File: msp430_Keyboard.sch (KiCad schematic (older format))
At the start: 10 parts, among them SW14 L_Super, SW4 L_Ctrl, SW48 R_Ctrl, SW5 L_Shift, SW53 R_Shift, SW57 Alt_GR, SW60 R_Super, SW61 FUNC, SW9 L_Alt, U1 MSP430F5510IRGZ

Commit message: USB-Connector und Vogelfutter
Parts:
- added C? (x2): C_Small, symbol Device:C_Small
- added J?: Conn_01x04_Male, symbol Connector:Conn_01x04_Male
- added R?: R_Small, symbol Device:R_Small
- added Y? (x2): Crystal_Small, symbol Device:Crystal_Small
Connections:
- net GND: now also U1.10 (AVSS1), U1.12 (DVSS1), U1.27 (DVSS2), U1.37 (VSSU), U1.44 (AVSS2), C?.2, C?.2, J?.4 (Pin_4)
- net +3V3: now reaches U1.11 (DVCC1)
- net +3V3: now also U1.28 (DVCC2), U1.42 (VUSB), U1.7 (AVCC1), J?.1 (Pin_1)
- net USB/D+: now reaches U1.38 (PU.0/DP)
- net USB/D+: now also R?.2
- net at U1.39 (PUR): now also R?.1
- net USB/D-: now reaches U1.40 (PU.1/DM)
- net VBUS: now reaches U1.41 (VBUS)
- net at U1.45 (P5.2/XT2IN): now also C?.1, Y?.1
- net at U1.46 (P5.3/XT2OUT): now also C?.1, Y?.2
- net at U1.47 (SBWTCK/TEST): now also J?.2 (Pin_2)
- net at U1.48 (~RST~/NMI/SBWTDIO): now also J?.3 (Pin_3)
- net at U1.8 (P5.4/XIN): now also Y?.1
- net at U1.9 (P5.5/XOUT): now also Y?.2

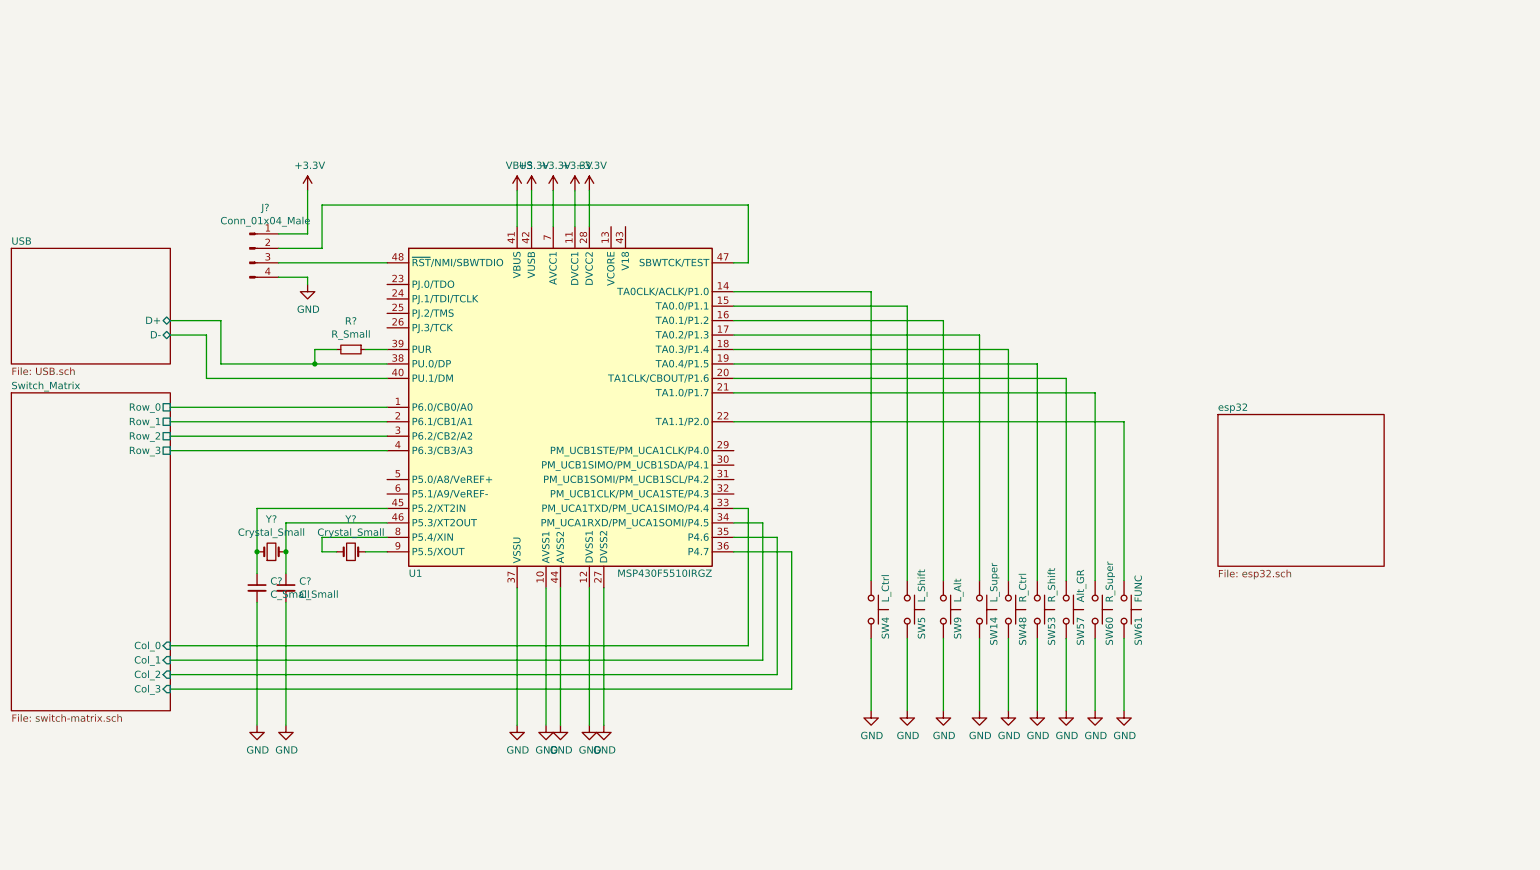
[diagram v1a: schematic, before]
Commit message: USB-Part und ESP32
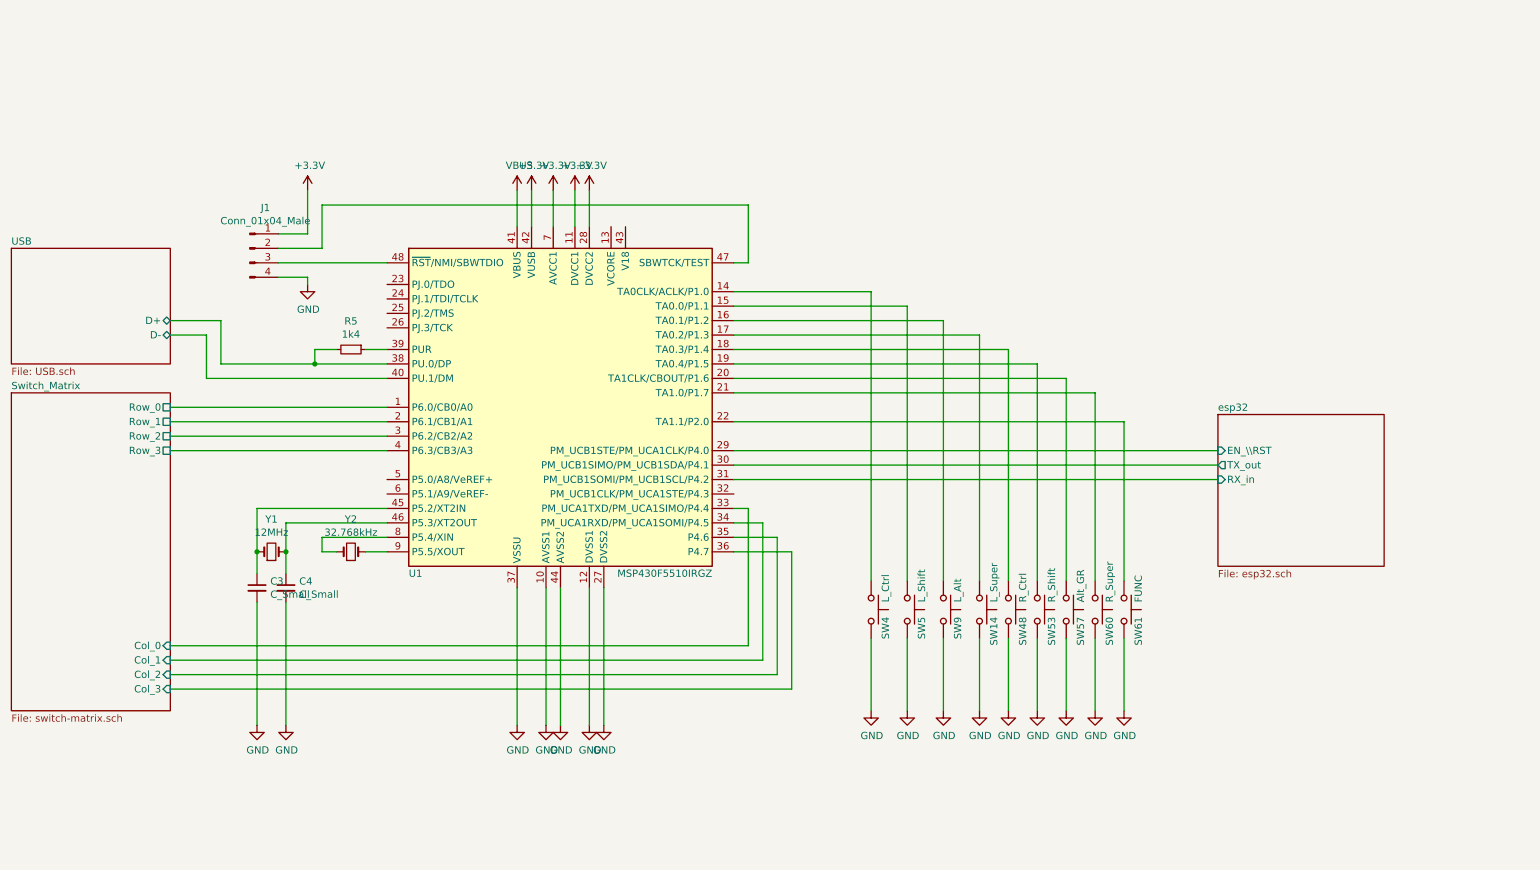
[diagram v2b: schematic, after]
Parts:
- C3, C4: renamed from C?; footprint (none) -> Capacitor_SMD:C_0603_1608Metric
- J1: renamed from J?; footprint (none) -> Connector_PinHeader_1.27mm:PinHeader_1x04_P1.27mm_Horizontal
- R5: renamed from R?; value R_Small -> 1k4; footprint (none) -> Resistor_SMD:R_0603_1608Metric
- Y1: renamed from Y?; value Crystal_Small -> 12MHz; footprint (none) -> Crystal:Crystal_SMD_EuroQuartz_MT-4Pin_3.2x2.5mm_HandSoldering
- Y2: renamed from Y?; value Crystal_Small -> 32.768kHz; footprint (none) -> Crystal:Crystal_SMD_MicroCrystal_MS3V-T1R
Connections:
- net esp32/EN_\\RST: now reaches U1.29 (PM_UCB1STE/PM_UCA1CLK/P4.0)
- net esp32/TX_out: now reaches U1.30 (PM_UCB1SIMO/PM_UCB1SDA/P4.1)
- net esp32/RX_in: now reaches U1.31 (PM_UCB1SOMI/PM_UCB1SCL/P4.2)
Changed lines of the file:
@@
 $Descr A4 11693 8268
 encoding utf-8
-Sheet 1 3
+Sheet 1 4
 Title ""
 Date ""
@@
 	2100 3450 2750 3450
 $Comp
-L power:GND #PWR?
+L power:GND #PWR0107
 U 1 1 60C6E7A3
 P 4150 5950
-F 0 "#PWR?" H 4150 5700 50  0001 C CNN
+F 0 "#PWR0107" H 4150 5700 50  0001 C CNN
 F 1 "GND" H 4155 5777 50  0000 C CNN
 F 2 "" H 4150 5950 50  0001 C CNN
@@
 $EndComp
 $Comp
-L power:GND #PWR?
+L power:GND #PWR0108
 U 1 1 60C6EAB5
 P 4350 5950
-F 0 "#PWR?" H 4350 5700 50  0001 C CNN
+F 0 "#PWR0108" H 4350 5700 50  0001 C CNN
 F 1 "GND" H 4355 5777 50  0000 C CNN
 F 2 "" H 4350 5950 50  0001 C CNN
@@
 $EndComp
 $Comp
-L power:GND #PWR?
+L power:GND #PWR0109
 U 1 1 60C6EDE3
 P 4450 5950
-F 0 "#PWR?" H 4450 5700 50  0001 C CNN
+F 0 "#PWR0109" H 4450 5700 50  0001 C CNN
 F 1 "GND" H 4455 5777 50  0000 C CNN
 F 2 "" H 4450 5950 50  0001 C CNN
@@
 $EndComp
 $Comp
-L power:GND #PWR?
+L power:GND #PWR0110
 U 1 1 60C6F39B
 P 4650 5950
-F 0 "#PWR?" H 4650 5700 50  0001 C CNN
+F 0 "#PWR0110" H 4650 5700 50  0001 C CNN
 F 1 "GND" H 4655 5777 50  0000 C CNN
 F 2 "" H 4650 5950 50  0001 C CNN
@@
 $EndComp
 $Comp
-L power:GND #PWR?
+L power:GND #PWR0111
 U 1 1 60C6F780
 P 4750 5950
-F 0 "#PWR?" H 4750 5700 50  0001 C CNN
+F 0 "#PWR0111" H 4750 5700 50  0001 C CNN
 F 1 "GND" H 4755 5777 50  0000 C CNN
 F 2 "" H 4750 5950 50  0001 C CNN
@@
 	4150 5950 4150 5000
 $Comp
-L Device:Crystal_Small Y?
+L Device:Crystal_Small Y2
 U 1 1 60C751AE
 P 3000 4750
-F 0 "Y?" H 3000 4975 50  0000 C CNN
-F 1 "Crystal_Small" H 3000 4884 50  0000 C CNN
-F 2 "" H 3000 4750 50  0001 C CNN
+F 0 "Y2" H 3000 4975 50  0000 C CNN
+F 1 "32.768kHz" H 3000 4884 50  0000 C CNN
+F 2 "Crystal:Crystal_SMD_MicroCrystal_MS3V-T1R" H 3000 4750 50  0001 C CNN
 F 3 "~" H 3000 4750 50  0001 C CNN
 	1    3000 4750
@@
 $EndComp
 $Comp
-L Device:Crystal_Small Y?
+L Device:Crystal_Small Y1
 U 1 1 60C76001
 P 2450 4750
-F 0 "Y?" H 2450 4975 50  0000 C CNN
-F 1 "Crystal_Small" H 2450 4884 50  0000 C CNN
-F 2 "" H 2450 4750 50  0001 C CNN
+F 0 "Y1" H 2450 4975 50  0000 C CNN
+F 1 "12MHz" H 2450 4884 50  0000 C CNN
+F 2 "Crystal:Crystal_SMD_EuroQuartz_MT-4Pin_3.2x2.5mm_HandSoldering" H 2450 4750 50  0001 C CNN
 F 3 "~" H 2450 4750 50  0001 C CNN
 	1    2450 4750
@@
 	2350 4450 2350 4750
 $Comp
-L Device:C_Small C?
+L Device:C_Small C3
 U 1 1 60C7B835
 P 2350 5000
-F 0 "C?" H 2442 5046 50  0000 L CNN
+F 0 "C3" H 2442 5046 50  0000 L CNN
 F 1 "C_Small" H 2442 4955 50  0000 L CNN
-F 2 "" H 2350 5000 50  0001 C CNN
+F 2 "Capacitor_SMD:C_0603_1608Metric" H 2350 5000 50  0001 C CNN
 F 3 "~" H 2350 5000 50  0001 C CNN
 	1    2350 5000
@@
 $EndComp
 $Comp
-L Device:C_Small C?
+L Device:C_Small C4
 U 1 1 60C7BD8A
 P 2550 5000
-F 0 "C?" H 2642 5046 50  0000 L CNN
+F 0 "C4" H 2642 5046 50  0000 L CNN
 F 1 "C_Small" H 2642 4955 50  0000 L CNN
-F 2 "" H 2550 5000 50  0001 C CNN
+F 2 "Capacitor_SMD:C_0603_1608Metric" H 2550 5000 50  0001 C CNN
 F 3 "~" H 2550 5000 50  0001 C CNN
 	1    2550 5000
@@
 Connection ~ 2550 4750
 $Comp
-L power:GND #PWR?
+L power:GND #PWR0112
 U 1 1 60C7EDC5
 P 2350 5950
-F 0 "#PWR?" H 2350 5700 50  0001 C CNN
+F 0 "#PWR0112" H 2350 5700 50  0001 C CNN
 F 1 "GND" H 2355 5777 50  0000 C CNN
 F 2 "" H 2350 5950 50  0001 C CNN
@@
 $EndComp
 $Comp
-L power:GND #PWR?
+L power:GND #PWR0113
 U 1 1 60C7F433
 P 2550 5950
-F 0 "#PWR?" H 2550 5700 50  0001 C CNN
+F 0 "#PWR0113" H 2550 5700 50  0001 C CNN
 F 1 "GND" H 2555 5777 50  0000 C CNN
 F 2 "" H 2550 5950 50  0001 C CNN
@@
 	2350 5100 2350 5950
 $Comp
-L Device:R_Small R?
+L Device:R_Small R5
 U 1 1 60C82900
 P 3000 3350
-F 0 "R?" V 2804 3350 50  0000 C CNN
-F 1 "R_Small" V 2895 3350 50  0000 C CNN
-F 2 "" H 3000 3350 50  0001 C CNN
+F 0 "R5" V 2804 3350 50  0000 C CNN
+F 1 "1k4" V 2895 3350 50  0000 C CNN
+F 2 "Resistor_SMD:R_0603_1608Metric" H 3000 3350 50  0001 C CNN
 F 3 "~" H 3000 3350 50  0001 C CNN
 	1    3000 3350
@@
 	2750 3450 3250 3450
 $Comp
-L Connector:Conn_01x04_Male J?
+L Connector:Conn_01x04_Male J1
 U 1 1 60C87E06
 P 2300 2650
-F 0 "J?" H 2408 2931 50  0000 C CNN
+F 0 "J1" H 2408 2931 50  0000 C CNN
 F 1 "Conn_01x04_Male" H 2408 2840 50  0000 C CNN
-F 2 "" H 2300 2650 50  0001 C CNN
+F 2 "Connector_PinHeader_1.27mm:PinHeader_1x04_P1.27mm_Horizontal" H 2300 2650 50  0001 C CNN
 F 3 "~" H 2300 2650 50  0001 C CNN
 	1    2300 2650
@@
 	2500 2750 3250 2750
 $Comp
-L power:GND #PWR?
+L power:GND #PWR0114
 U 1 1 60C8AB36
 P 2700 2900
-F 0 "#PWR?" H 2700 2650 50  0001 C CNN
+F 0 "#PWR0114" H 2700 2650 50  0001 C CNN
 F 1 "GND" H 2705 2727 50  0000 C CNN
 F 2 "" H 2700 2900 50  0001 C CNN
@@
 	5750 2750 5650 2750
 $Comp
-L power:+3.3V #PWR?
+L power:+3.3V #PWR0115
 U 1 1 60C98CCE
 P 2700 2250
-F 0 "#PWR?" H 2700 2100 50  0001 C CNN
+F 0 "#PWR0115" H 2700 2100 50  0001 C CNN
 F 1 "+3.3V" H 2715 2423 50  0000 C CNN
 F 2 "" H 2700 2250 50  0001 C CNN
@@
 	2700 2550 2500 2550
 $Comp
-L power:VBUS #PWR?
+L power:VBUS #PWR0116
 U 1 1 60C9B836
 P 4150 2250
-F 0 "#PWR?" H 4150 2100 50  0001 C CNN
+F 0 "#PWR0116" H 4150 2100 50  0001 C CNN
 F 1 "VBUS" H 4165 2423 50  0000 C CNN
 F 2 "" H 4150 2250 50  0001 C CNN
@@
 	4150 2250 4150 2500
 $Comp
-L power:+3.3V #PWR?
+L power:+3.3V #PWR0117
 U 1 1 60CA1020
 P 4250 2250
-F 0 "#PWR?" H 4250 2100 50  0001 C CNN
+F 0 "#PWR0117" H 4250 2100 50  0001 C CNN
 F 1 "+3.3V" H 4265 2423 50  0000 C CNN
 F 2 "" H 4250 2250 50  0001 C CNN
@@
 $EndComp
 $Comp
-L power:+3.3V #PWR?
+L power:+3.3V #PWR0118
 U 1 1 60CA142C
 P 4400 2250
-F 0 "#PWR?" H 4400 2100 50  0001 C CNN
+F 0 "#PWR0118" H 4400 2100 50  0001 C CNN
 F 1 "+3.3V" H 4415 2423 50  0000 C CNN
 F 2 "" H 4400 2250 50  0001 C CNN
@@
 $EndComp
 $Comp
-L power:+3.3V #PWR?
+L power:+3.3V #PWR0119
 U 1 1 60CA1866
 P 4550 2250
-F 0 "#PWR?" H 4550 2100 50  0001 C CNN
+F 0 "#PWR0119" H 4550 2100 50  0001 C CNN
 F 1 "+3.3V" H 4565 2423 50  0000 C CNN
 F 2 "" H 4550 2250 50  0001 C CNN
@@
 $EndComp
 $Comp
-L power:+3.3V #PWR?
+L power:+3.3V #PWR0120
 U 1 1 60CA1CCE
 P 4650 2250
-F 0 "#PWR?" H 4650 2100 50  0001 C CNN
+F 0 "#PWR0120" H 4650 2100 50  0001 C CNN
 F 1 "+3.3V" H 4665 2423 50  0000 C CNN
 F 2 "" H 4650 2250 50  0001 C CNN
@@
 F0 "esp32" 50
 F1 "esp32.sch" 50
+F2 "EN_\\RST" I L 9000 4050 50
+F3 "TX_out" O L 9000 4150 50
+F4 "RX_in" I L 9000 4250 50
 $EndSheet
+Wire Wire Line
+	5650 4050 9000 4050
+Wire Wire Line
+	9000 4150 5650 4150
+Wire Wire Line
+	5650 4250 9000 4250
 $EndSCHEMATC

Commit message: Rotary Encoder added
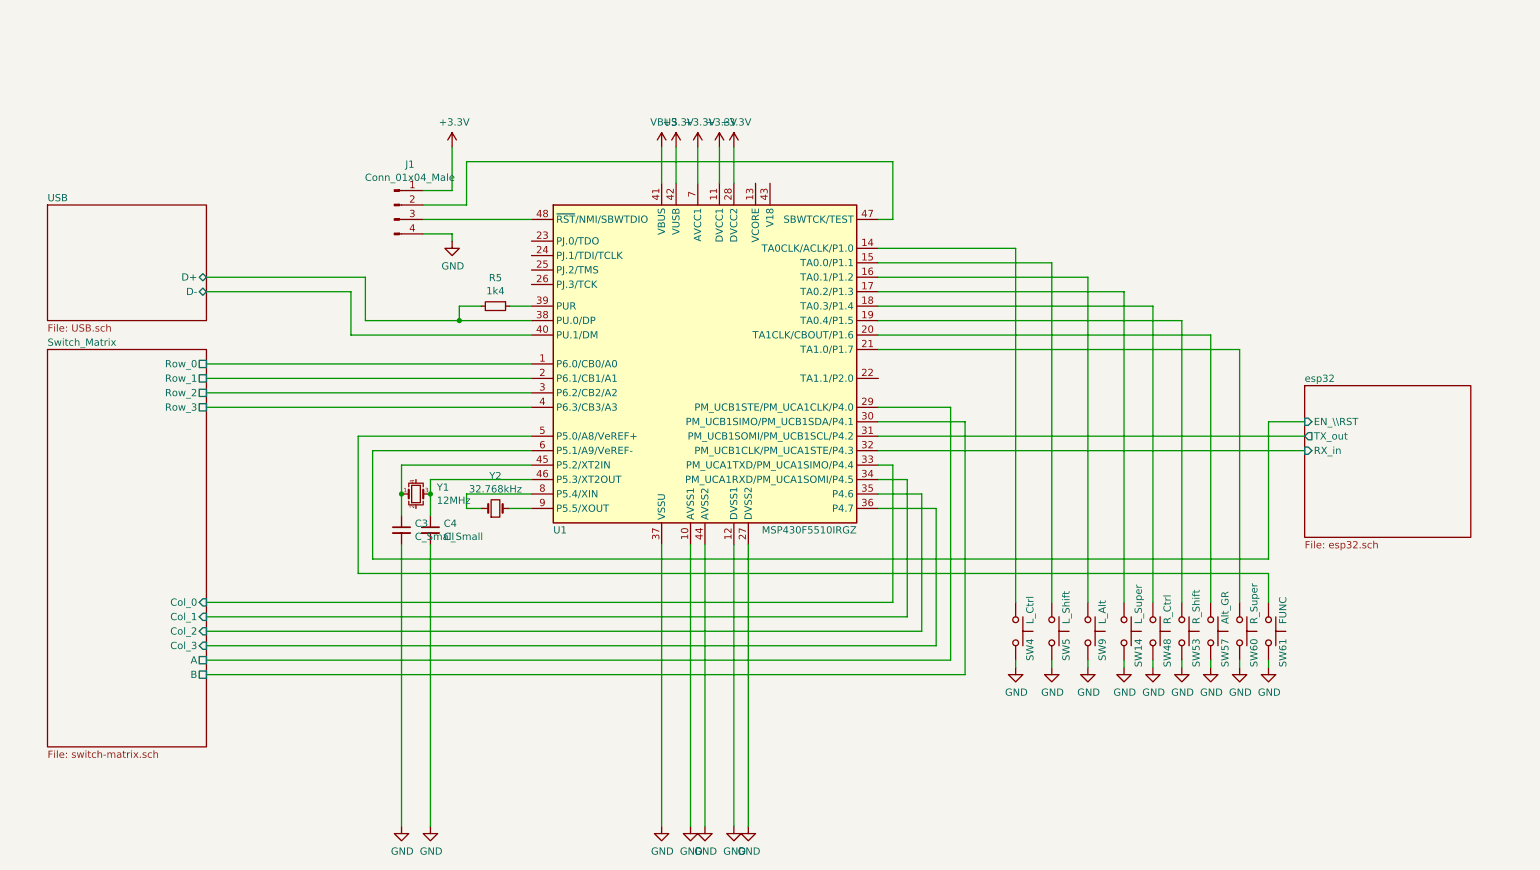
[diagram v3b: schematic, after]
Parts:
- removed Y1: 12MHz, Crystal:Crystal_SMD_EuroQuartz_MT-4Pin_3.2x2.5mm_HandSoldering, symbol Device:Crystal_Small
- added Y1: 12MHz, Crystal:Crystal_SMD_3225-4Pin_3.2x2.5mm, symbol Device:Crystal_GND24_Small
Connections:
- net esp32/EN_\\RST: now also U1.6 (P5.1/A9/VeREF-); no longer U1.29 (PM_UCB1STE/PM_UCA1CLK/P4.0)
- net esp32/RX_in: now also U1.32 (PM_UCB1CLK/PM_UCA1STE/P4.3); no longer U1.31 (PM_UCB1SOMI/PM_UCB1SCL/P4.2)
- net esp32/TX_out: now also U1.31 (PM_UCB1SOMI/PM_UCB1SCL/P4.2); no longer U1.30 (PM_UCB1SIMO/PM_UCB1SDA/P4.1)
- net at U1.22 (TA1.1/P2.0): no longer SW61.1
- net at C3.1, U1.45 (P5.2/XT2IN): now also Y1.1
- net at C4.1, U1.46 (P5.3/XT2OUT): now also Y1.3
- net at U1.5 (P5.0/A8/VeREF+): now also SW61.1
- new net Switch_Matrix/A: U1.29 (PM_UCB1STE/PM_UCA1CLK/P4.0)
- new net Switch_Matrix/B: U1.30 (PM_UCB1SIMO/PM_UCB1SDA/P4.1)
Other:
- moved on the sheet: C3, C4, J1, R5, SW14, SW4, SW48, SW5, SW53, SW57, SW60, SW61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

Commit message: Routing angefangen
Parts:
- added C10, C18: 220n, Capacitor_SMD:C_0603_1608Metric_Pad1.08x0.95mm_HandSolder, symbol Device:C_Small
- added C11, C13, C15: 100n, Capacitor_SMD:C_0603_1608Metric_Pad1.08x0.95mm_HandSolder, symbol Device:C_Small
- added C12, C14, C16: 10µ, Capacitor_SMD:C_1206_3216Metric_Pad1.33x1.80mm_HandSolder, symbol Device:C_Small
- added C17: 470n, Capacitor_SMD:C_0603_1608Metric_Pad1.08x0.95mm_HandSolder, symbol Device:C_Small
- added JP1: Jumper_NC_Small, Jumper:SolderJumper-2_P1.3mm_Bridged2Bar_RoundedPad1.0x1.5mm, symbol Device:Jumper_NC_Small
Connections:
- net +3V3: now also C11.1, C12.1, C13.1, C14.1, C15.1, C16.1, JP1.2; no longer U1.42 (VUSB)
- net GND: now also C10.2, C11.2, C12.2, C13.2, C14.2, C15.2, C16.2, C17.2, C18.2
- net at U1.13 (VCORE): now also C17.1
- net at U1.43 (V18): now also C18.1
- net at U1.8 (P5.4/XIN): now also Y2.2; no longer Y2.1
- net at U1.9 (P5.5/XOUT): now also Y2.1; no longer Y2.2
- new net: C10.1, JP1.1, U1.42 (VUSB)
